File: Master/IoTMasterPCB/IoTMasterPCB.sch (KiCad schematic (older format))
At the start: 0 parts

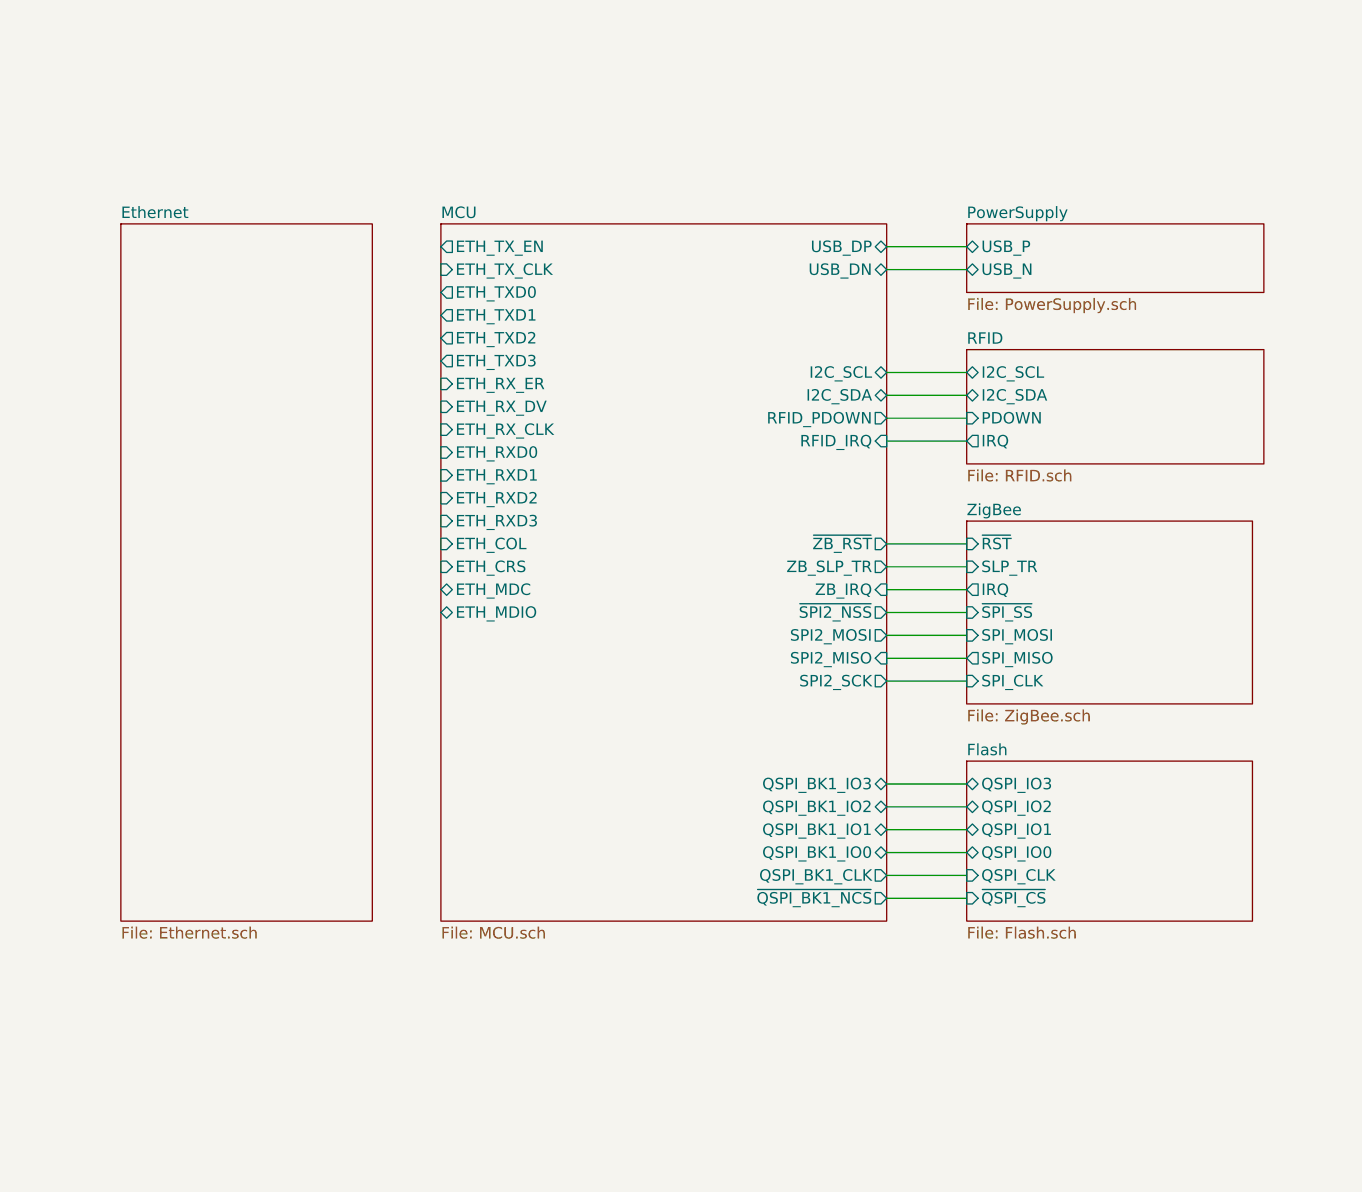
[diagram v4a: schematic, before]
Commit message: Finished RFID and Ethernet circuits.
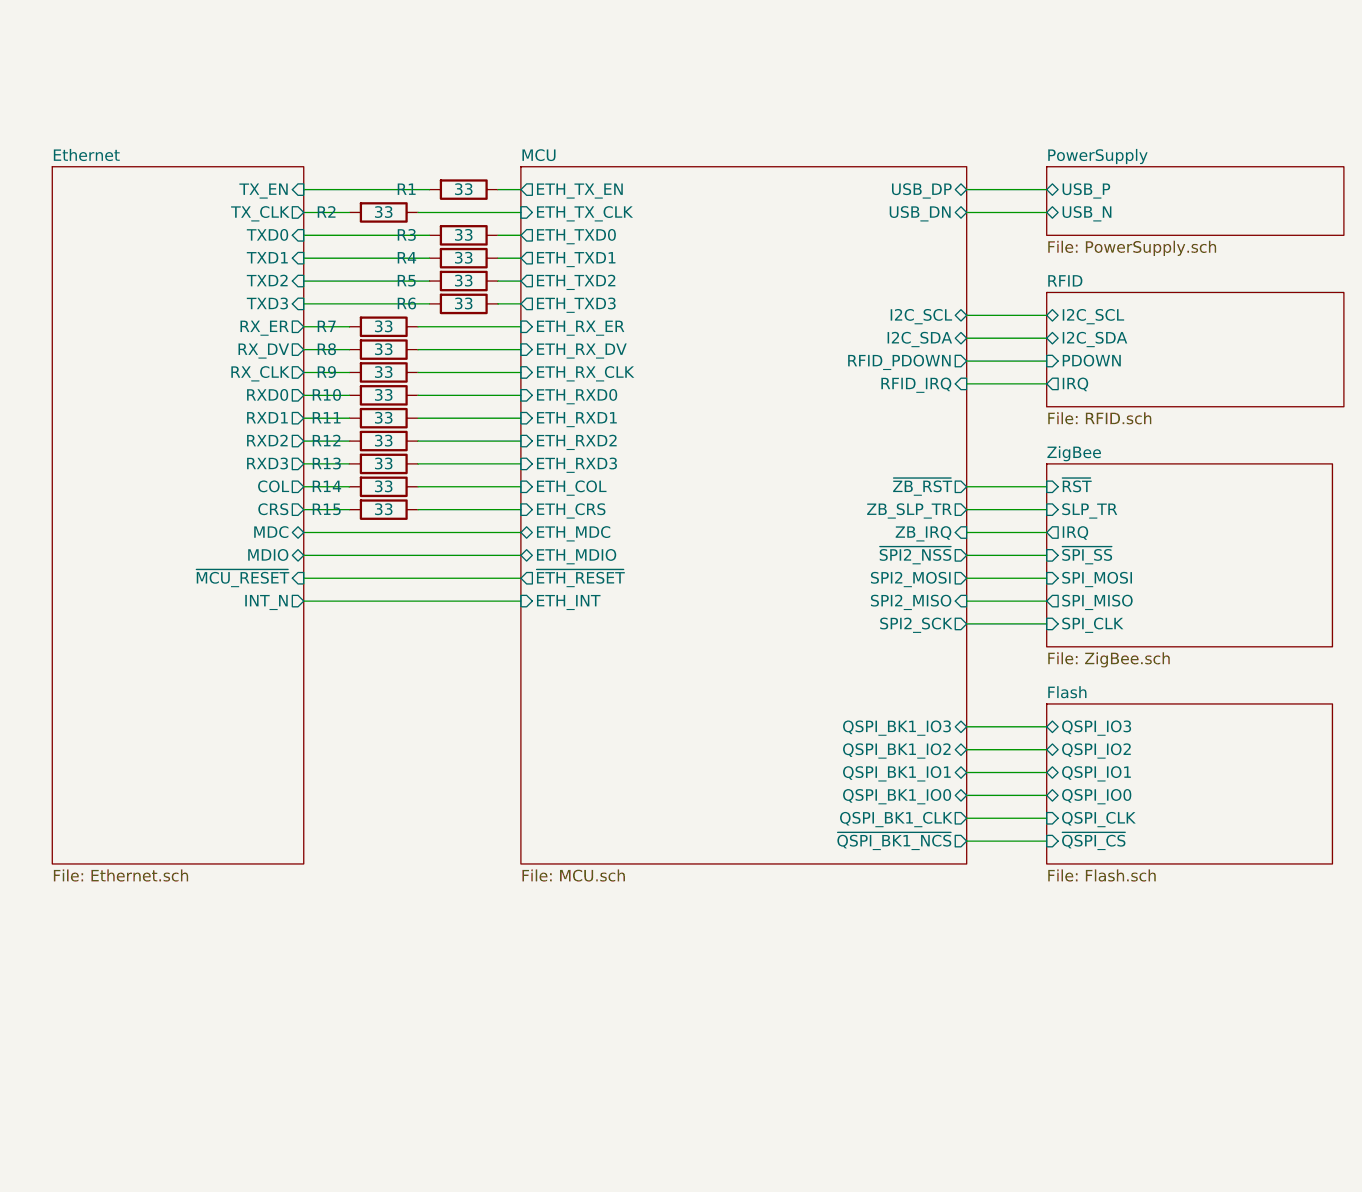
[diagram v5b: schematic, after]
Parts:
- added R1, R10, R11, R12, R13, R14, R15, R2, R3, R4, R5, R6, R7, R8, R9: 33, Resistor_SMD:R_0603_1608Metric, symbol Device:R
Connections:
- net MCU/ETH_COL: now also R14.1
- net MCU/ETH_CRS: now also R15.1
- net MCU/ETH_RXD0: now also R10.1
- net MCU/ETH_RXD1: now also R11.1
- net MCU/ETH_RXD2: now also R12.1
- net MCU/ETH_RXD3: now also R13.1
- net MCU/ETH_RX_CLK: now also R9.1
- net MCU/ETH_RX_DV: now also R8.1
- net MCU/ETH_RX_ER: now also R7.1
- net MCU/ETH_TXD0: now also R3.1
- net MCU/ETH_TXD1: now also R4.1
- net MCU/ETH_TXD2: now also R5.1
- net MCU/ETH_TXD3: now also R6.1
- net MCU/ETH_TX_CLK: now also R2.1
- net MCU/ETH_TX_EN: now also R1.1
- new net Ethernet/COL: R14.2
- new net Ethernet/CRS: R15.2
- new net Ethernet/RXD0: R10.2
- new net Ethernet/RXD1: R11.2
- new net Ethernet/RXD2: R12.2
- new net Ethernet/RXD3: R13.2
- new net Ethernet/RX_CLK: R9.2
- new net Ethernet/RX_DV: R8.2
- new net Ethernet/RX_ER: R7.2
- new net Ethernet/TXD0: R3.2
- new net Ethernet/TXD1: R4.2
- new net Ethernet/TXD2: R5.2
- new net Ethernet/TXD3: R6.2
- new net Ethernet/TX_CLK: R2.2
- new net Ethernet/TX_EN: R1.2

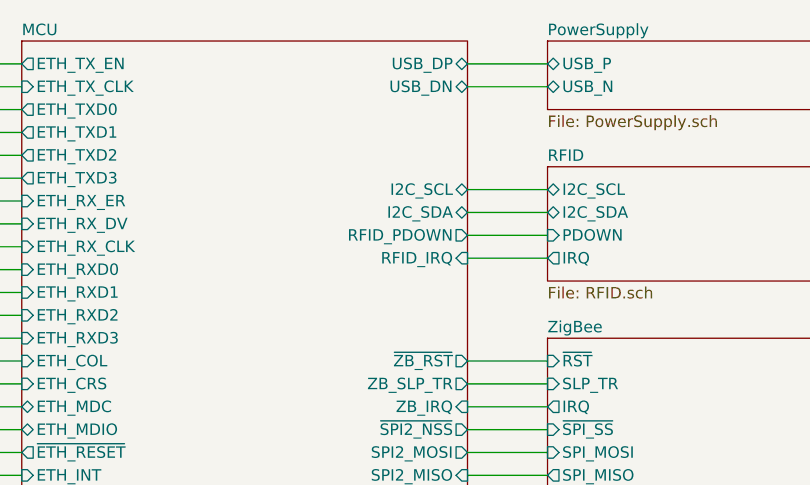
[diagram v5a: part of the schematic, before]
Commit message: Placed STM32 on Master PCB. Corrected I2C naming.
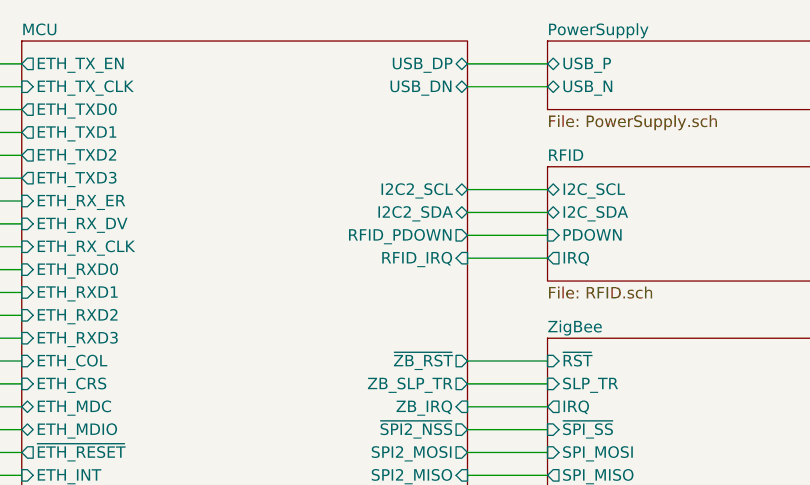
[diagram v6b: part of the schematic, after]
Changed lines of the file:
@@
 F15 "QSPI_BK1_IO2" B R 6900 4500 50
 F16 "QSPI_BK1_IO3" B R 6900 4400 50
-F17 "I2C_SCL" B R 6900 2600 50
-F18 "I2C_SDA" B R 6900 2700 50
+F17 "I2C2_SCL" B R 6900 2600 50
+F18 "I2C2_SDA" B R 6900 2700 50
 F19 "RFID_PDOWN" O R 6900 2800 50
 F20 "RFID_IRQ" I R 6900 2900 50
